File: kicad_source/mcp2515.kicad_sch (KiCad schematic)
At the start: 13 parts, among them CN4 GH_SM04B-GHS-TB, CN5 GH_SM04B-GHS-TB, U8 MCP2515, U9 SN65HVD232, Y1 16MHz

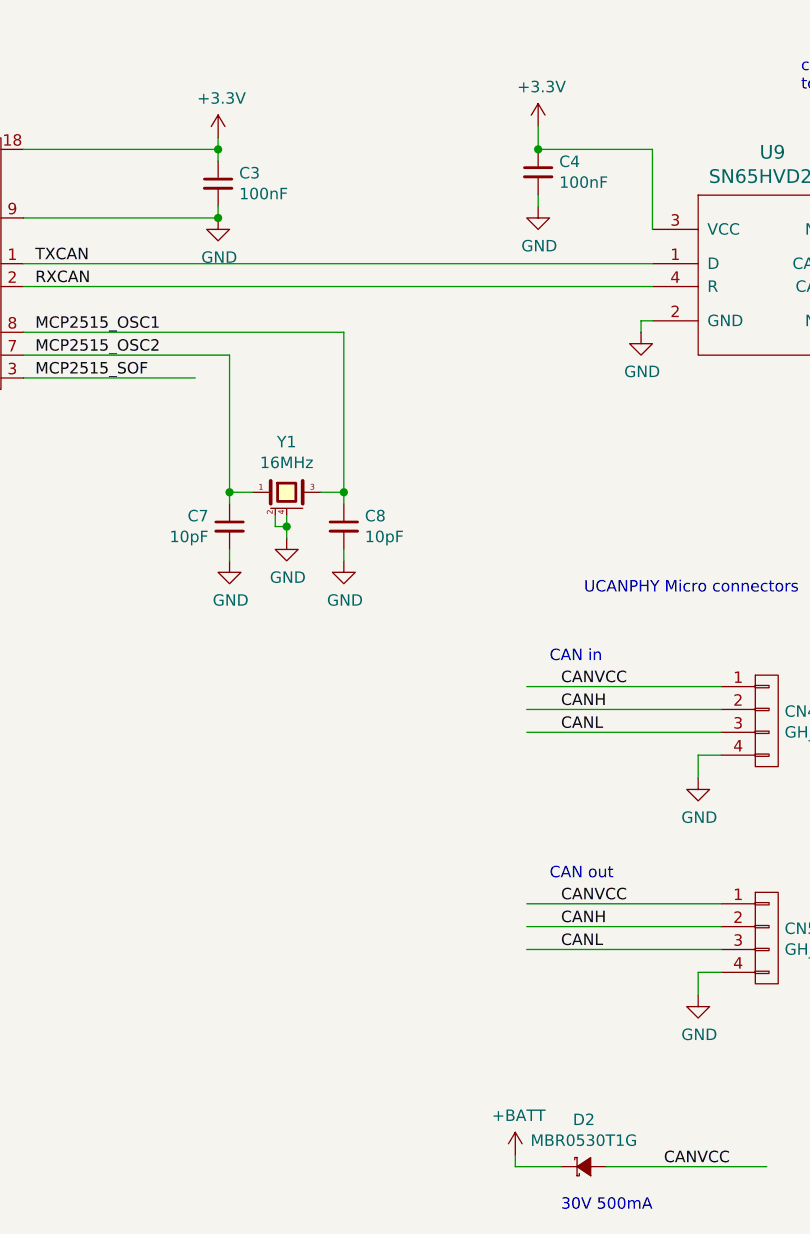
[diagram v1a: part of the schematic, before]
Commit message: reworked library references
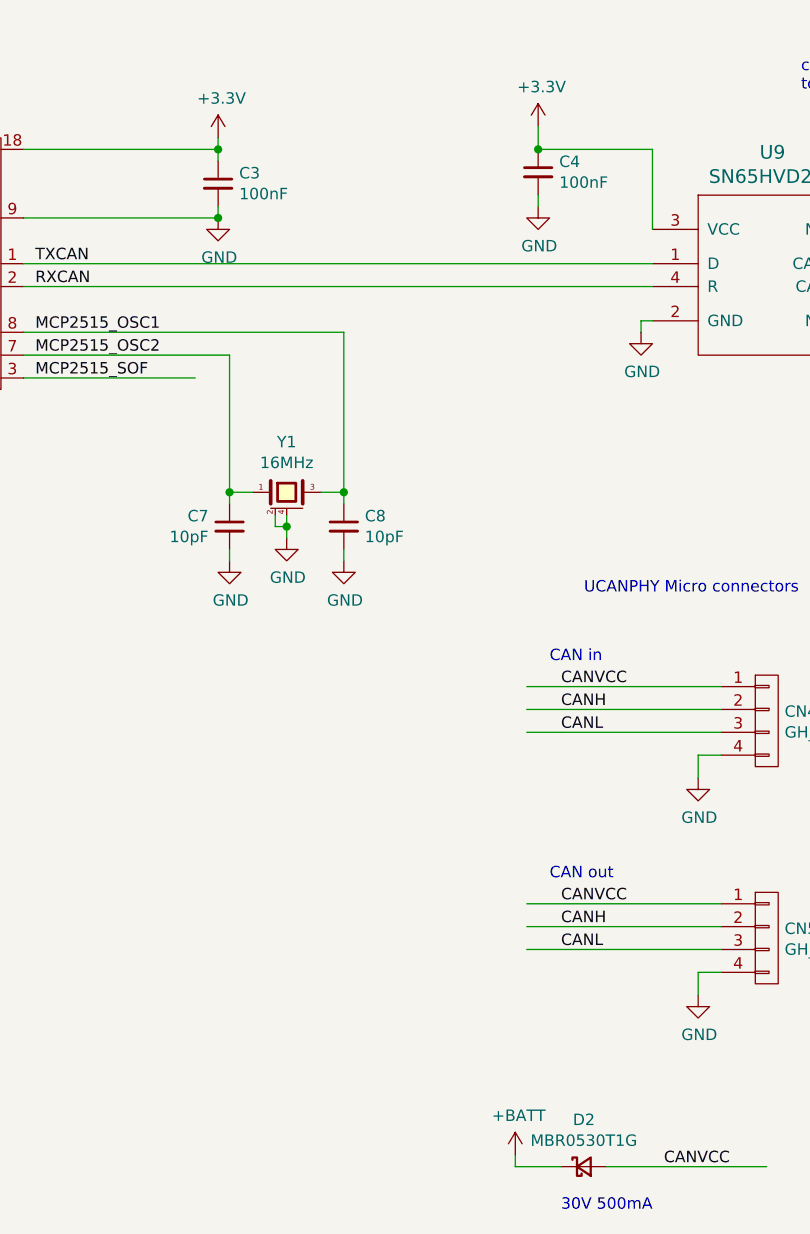
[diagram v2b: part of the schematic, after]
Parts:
- C3, C4, C7, C8: footprint capacitors:C_0603 -> Capacitor_SMD:C_0603_1608Metric; symbol OpenCyphalPicoBase-rescue:C_0603-devices -> Device:C_Small
- D2: footprint diodes:SOD-123 -> Diode_SMD:D_SOD-123; symbol OpenCyphalPicoBase-rescue:D_Schottky_Small-devices -> Device:D_Schottky_Small
- R1, R2, R3: footprint resistors:R_0603 -> Resistor_SMD:R_0603_1608Metric; symbol OpenCyphalPicoBase-rescue:R_0603-devices -> Device:R_Small
- U8: footprint SOIC:SOIC-18_7.5x11.6mm_Pitch1.27mm -> Package_SO:SOIC-18W_7.5x11.6mm_P1.27mm
- U9: footprint SOIC:SOIC-8_3.9x4.9mm_Pitch1.27mm -> Package_SO:SOIC-8_3.9x4.9mm_P1.27mm
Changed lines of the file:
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@@
     (property "Reference" "U8" (id 0) (at 127 37.465 0))
     (property "Value" "MCP2515" (id 1) (at 127 39.7764 0))
-    (property "Footprint" "SOIC:SOIC-18_7.5x11.6mm_Pitch1.27mm" (id 2) (at 127 55.88 0)
+    (property "Footprint" "Package_SO:SOIC-18W_7.5x11.6mm_P1.27mm" (id 2) (at 127 55.88 0)
       (effects (font (size 1.27 1.27)) hide)
     )
@@
     (pin "9")
   )
-  (symbol (lib_id "OpenCyphalPicoBase-rescue:C_0603-devices") (at 162.56 46.99 0) (unit 1)
+  (symbol (lib_id "Device:C_Small") (at 162.56 46.99 0) (unit 1)
     (in_bom yes) (on_board yes)
     (property "Reference" "C3" (id 0) (at 164.8968 45.8216 0)
@@
       (effects (font (size 1.27 1.27)) (justify left))
     )
-    (property "Footprint" "capacitors:C_0603" (id 2) (at 162.56 50.8 0)
+    (property "Footprint" "Capacitor_SMD:C_0603_1608Metric" (id 2) (at 162.56 50.8 0)
       (effects (font (size 1.27 1.27)) hide)
     )
@@
     (pin "1")
   )
-  (symbol (lib_id "OpenCyphalPicoBase-rescue:R_0603-devices") (at 87.63 38.1 0) (unit 1)
+  (symbol (lib_id "Device:R_Small") (at 87.63 38.1 0) (unit 1)
     (in_bom yes) (on_board yes)
     (property "Reference" "R3" (id 0) (at 89.1286 36.9316 0)
@@
       (effects (font (size 1.27 1.27)) (justify left))
     )
-    (property "Footprint" "resistors:R_0603" (id 2) (at 87.63 41.91 0)
+    (property "Footprint" "Resistor_SMD:R_0603_1608Metric" (id 2) (at 87.63 41.91 0)
       (effects (font (size 1.27 1.27)) hide)
     )
@@
     (pin "1")
   )
-  (symbol (lib_id "OpenCyphalPicoBase-rescue:R_0603-devices") (at 80.01 38.1 0) (unit 1)
+  (symbol (lib_id "Device:R_Small") (at 80.01 38.1 0) (unit 1)
     (in_bom yes) (on_board yes)
     (property "Reference" "R2" (id 0) (at 81.5086 36.9316 0)
@@
       (effects (font (size 1.27 1.27)) (justify left))
     )
-    (property "Footprint" "resistors:R_0603" (id 2) (at 80.01 41.91 0)
+    (property "Footprint" "Resistor_SMD:R_0603_1608Metric" (id 2) (at 80.01 41.91 0)
       (effects (font (size 1.27 1.27)) hide)
     )
@@
     (pin "1")
   )
-  (symbol (lib_id "OpenCyphalPicoBase-rescue:R_0603-devices") (at 72.39 38.1 0) (unit 1)
+  (symbol (lib_id "Device:R_Small") (at 72.39 38.1 0) (unit 1)
     (in_bom yes) (on_board yes)
     (property "Reference" "R1" (id 0) (at 73.8886 36.9316 0)
@@
       (effects (font (size 1.27 1.27)) (justify left))
     )
-    (property "Footprint" "resistors:R_0603" (id 2) (at 72.39 41.91 0)
+    (property "Footprint" "Resistor_SMD:R_0603_1608Metric" (id 2) (at 72.39 41.91 0)
       (effects (font (size 1.27 1.27)) hide)
     )
@@
       (effects (font (size 1.524 1.524)))
     )
-    (property "Footprint" "SOIC:SOIC-8_3.9x4.9mm_Pitch1.27mm" (id 2) (at 232.41 67.31 0)
+    (property "Footprint" "Package_SO:SOIC-8_3.9x4.9mm_P1.27mm" (id 2) (at 232.41 67.31 0)
       (effects (font (size 1.524 1.524)) hide)
     )
@@
     (pin "8")
   )
-  (symbol (lib_id "OpenCyphalPicoBase-rescue:C_0603-devices") (at 198.12 45.72 0) (unit 1)
+  (symbol (lib_id "Device:C_Small") (at 198.12 45.72 0) (unit 1)
     (in_bom yes) (on_board yes)
     (property "Reference" "C4" (id 0) (at 200.4568 44.5516 0)
@@
       (effects (font (size 1.27 1.27)) (justify left))
     )
-    (property "Footprint" "capacitors:C_0603" (id 2) (at 198.12 49.53 0)
+    (property "Footprint" "Capacitor_SMD:C_0603_1608Metric" (id 2) (at 198.12 49.53 0)
       (effects (font (size 1.27 1.27)) hide)
     )
@@
     (pin "1")
   )
-  (symbol (lib_id "OpenCyphalPicoBase-rescue:D_Schottky_Small-devices") (at 203.2 156.21 0) (unit 1)
+  (symbol (lib_id "Device:D_Schottky_Small") (at 203.2 156.21 0) (unit 1)
     (in_bom yes) (on_board yes)
     (property "Reference" "D2" (id 0) (at 203.2 151.003 0))
     (property "Value" "MBR0530T1G" (id 1) (at 203.2 153.3144 0))
-    (property "Footprint" "diodes:SOD-123" (id 2) (at 203.2 156.21 90)
+    (property "Footprint" "Diode_SMD:D_SOD-123" (id 2) (at 203.2 156.21 90)
       (effects (font (size 1.27 1.27)) hide)
     )
@@
     (pin "2")
   )
-  (symbol (lib_id "OpenCyphalPicoBase-rescue:C_0603-devices") (at 176.53 85.09 0) (unit 1)
+  (symbol (lib_id "Device:C_Small") (at 176.53 85.09 0) (unit 1)
     (in_bom yes) (on_board yes)
     (property "Reference" "C8" (id 0) (at 178.8668 83.9216 0)
@@
       (effects (font (size 1.27 1.27)) (justify left))
     )
-    (property "Footprint" "capacitors:C_0603" (id 2) (at 176.53 88.9 0)
+    (property "Footprint" "Capacitor_SMD:C_0603_1608Metric" (id 2) (at 176.53 88.9 0)
       (effects (font (size 1.27 1.27)) hide)
     )
@@
     (pin "2")
   )
-  (symbol (lib_id "OpenCyphalPicoBase-rescue:C_0603-devices") (at 163.83 85.09 0) (mirror y) (unit 1)
+  (symbol (lib_id "Device:C_Small") (at 163.83 85.09 0) (mirror y) (unit 1)
     (in_bom yes) (on_board yes)
     (property "Reference" "C7" (id 0) (at 161.4932 83.9216 0)
@@
       (effects (font (size 1.27 1.27)) (justify left))
     )
-    (property "Footprint" "capacitors:C_0603" (id 2) (at 163.83 88.9 0)
-      (effects (font (size 1.27 1.27)) hide)
-    )
+    (property "Footprint" "Capacitor_SMD:C_0603_1608Metric" (id 2) (at 163.83 88.9 0)
+      (effects (font (size 1.27 1.27)) hide)
+    )

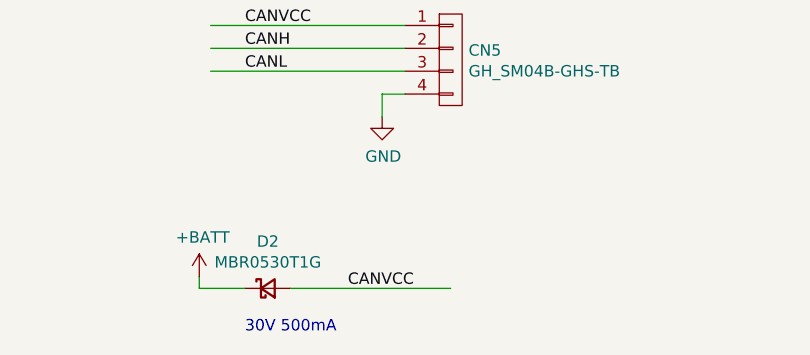
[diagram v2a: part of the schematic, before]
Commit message: added poly fuse
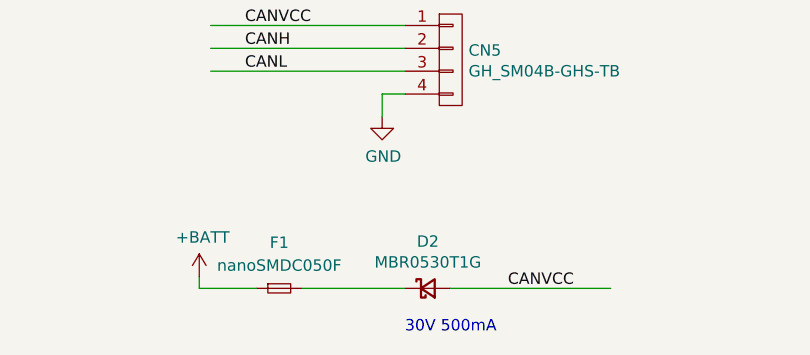
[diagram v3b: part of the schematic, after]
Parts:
- added F1: nanoSMDC050F, Fuse:Fuse_1206_3216Metric, symbol Device:Fuse_Small
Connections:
- net +BATT: now also F1.1; no longer D2.1 (K)
- new net: D2.1 (K), F1.2
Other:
- moved on the sheet: D2
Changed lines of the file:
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@@
     (stroke (width 0) (type default) (color 0 0 0 0))
   )
-  (wire (pts (xy 223.52 156.21) (xy 205.74 156.21))
+  (wire (pts (xy 241.3 156.21) (xy 223.52 156.21))
+    (stroke (width 0) (type default) (color 0 0 0 0))
+  )
+  (wire (pts (xy 207.01 156.21) (xy 218.44 156.21))
     (stroke (width 0) (type default) (color 0 0 0 0))
   )
@@
     (stroke (width 0) (type default) (color 0 0 0 0))
   )
-  (wire (pts (xy 195.58 156.21) (xy 200.66 156.21))
-    (stroke (width 0) (type default) (color 0 0 0 0))
-  )
   (wire (pts (xy 215.9 110.49) (xy 215.9 113.03))
     (stroke (width 0) (type default) (color 0 0 0 0))
@@
     (stroke (width 0) (type default) (color 0 0 0 0))
   )
+  (wire (pts (xy 195.58 156.21) (xy 201.93 156.21))
+    (stroke (width 0) (type default) (color 0 0 0 0))
+  )
   (wire (pts (xy 210.82 43.18) (xy 210.82 52.07))
     (stroke (width 0) (type default) (color 0 0 0 0))
@@
     (effects (font (size 1.27 1.27)) (justify left bottom))
   )
-  (text "30V 500mA" (at 200.66 161.29 0)
+  (text "30V 500mA" (at 218.44 161.29 0)
     (effects (font (size 1.27 1.27)) (justify left bottom))
   )
@@
     (effects (font (size 1.27 1.27)) (justify left bottom))
   )
-  (label "CANVCC" (at 212.09 156.21 0)
+  (label "CANVCC" (at 229.87 156.21 0)
     (effects (font (size 1.27 1.27)) (justify left bottom))
   )
@@
     (pin "1")
   )
-  (symbol (lib_id "Device:D_Schottky_Small") (at 203.2 156.21 0) (unit 1)
-    (in_bom yes) (on_board yes)
-    (property "Reference" "D2" (id 0) (at 203.2 151.003 0))
-    (property "Value" "MBR0530T1G" (id 1) (at 203.2 153.3144 0))
-    (property "Footprint" "Diode_SMD:D_SOD-123" (id 2) (at 203.2 156.21 90)
-      (effects (font (size 1.27 1.27)) hide)
-    )
-    (property "Datasheet" "" (id 3) (at 203.2 156.21 90))
+  (symbol (lib_id "Device:D_Schottky_Small") (at 220.98 156.21 0) (unit 1)
+    (in_bom yes) (on_board yes)
+    (property "Reference" "D2" (id 0) (at 220.98 151.003 0))
+    (property "Value" "MBR0530T1G" (id 1) (at 220.98 153.3144 0))
+    (property "Footprint" "Diode_SMD:D_SOD-123" (id 2) (at 220.98 156.21 90)
+      (effects (font (size 1.27 1.27)) hide)
+    )
+    (property "Datasheet" "" (id 3) (at 220.98 156.21 90))
     (pin "1")
     (pin "2")
@@
     (pin "1")
   )
+  (symbol (lib_id "Device:Fuse_Small") (at 204.47 156.21 0) (unit 1)
+    (in_bom yes) (on_board yes) (fields_autoplaced)
+    (property "Reference" "F1" (id 0) (at 204.47 151.13 0))
+    (property "Value" "nanoSMDC050F" (id 1) (at 204.47 153.67 0))
+    (property "Footprint" "Fuse:Fuse_1206_3216Metric" (id 2) (at 204.47 156.21 0)
+      (effects (font (size 1.27 1.27)) hide)
+    )
+    (property "Datasheet" "~" (id 3) (at 204.47 156.21 0)
+      (effects (font (size 1.27 1.27)) hide)
+    )
+    (pin "1")
+    (pin "2")
+  )
 )
